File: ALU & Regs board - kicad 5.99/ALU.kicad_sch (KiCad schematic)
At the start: 50 parts, among them U1 74F381, U10 MC74ACT244DWG, U11 MC74ACT244DWG, U12 MC74ACT04DG, U13 MC74SCT00DG, U14 MC74ACT32DG, U15 MC74ACT02DG, U16 MC74ACT157DG, U17 MC74ACT153DG, U18 MC74ACT153DG, U19 MC74ACT08DG, U2 74F381, U20 MC74ACT20DG, U21 MC74ACT02DG, U22 MC74ACT02DG, U3 74F381, U4 74F382, U5 74F382, U6 74F182, U7 MC74ACT244DWG, U8 MC74ACT244DWG, U9 MC74ACT244DWG

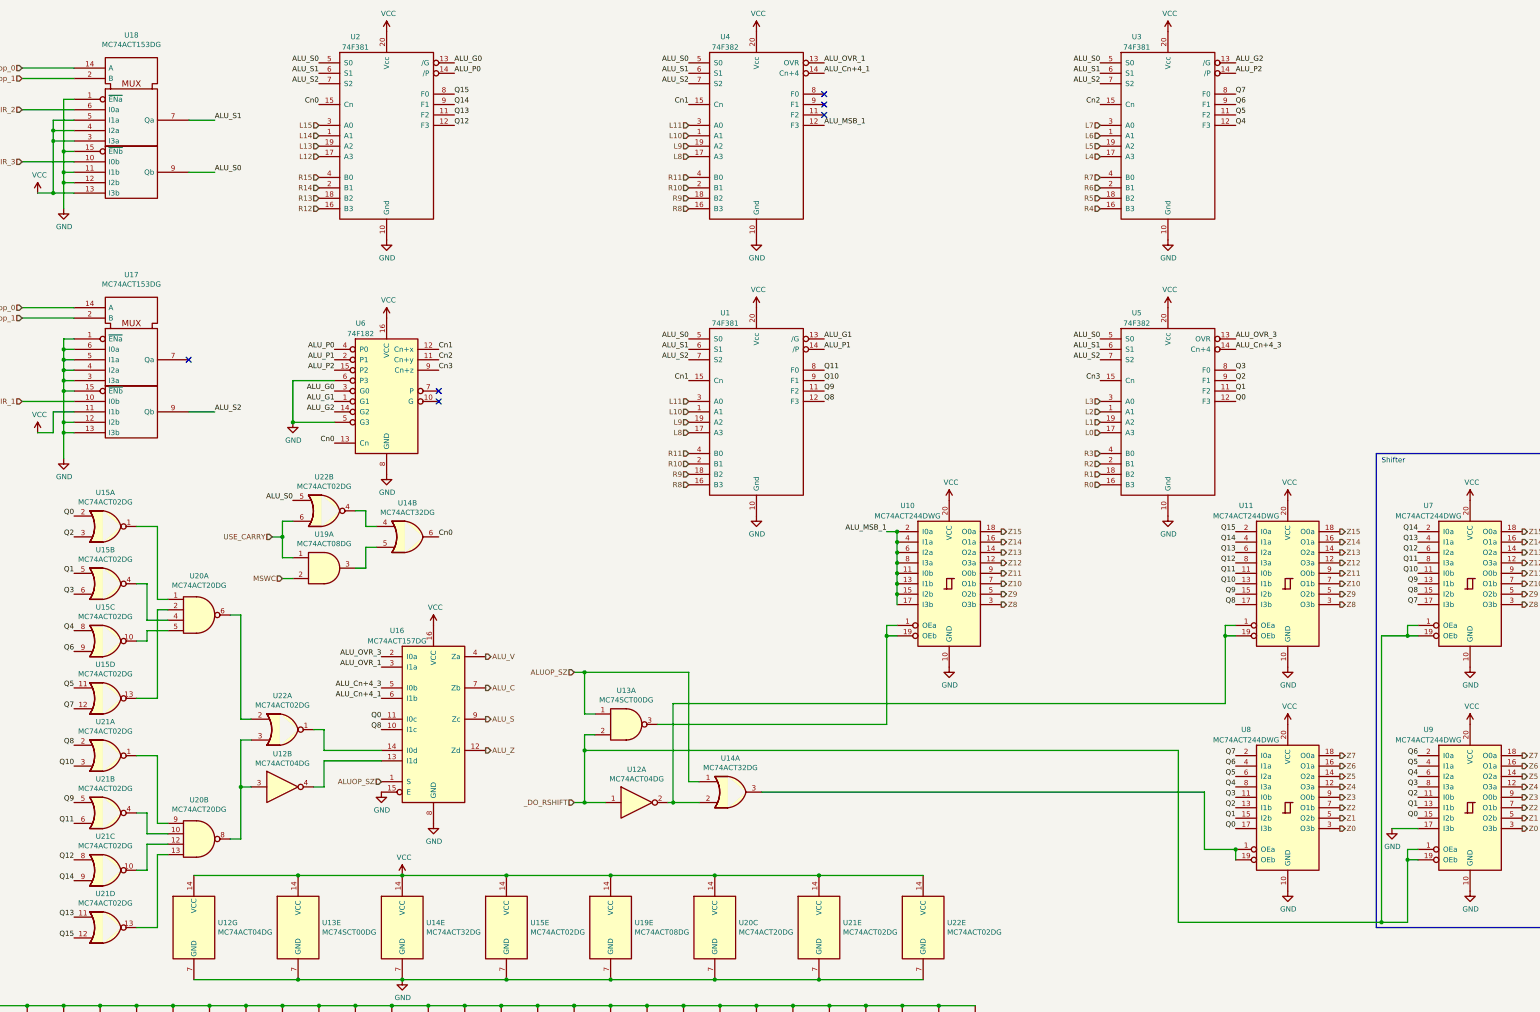
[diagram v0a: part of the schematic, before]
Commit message: added a buffer on the _RESET line, which is rather loaded
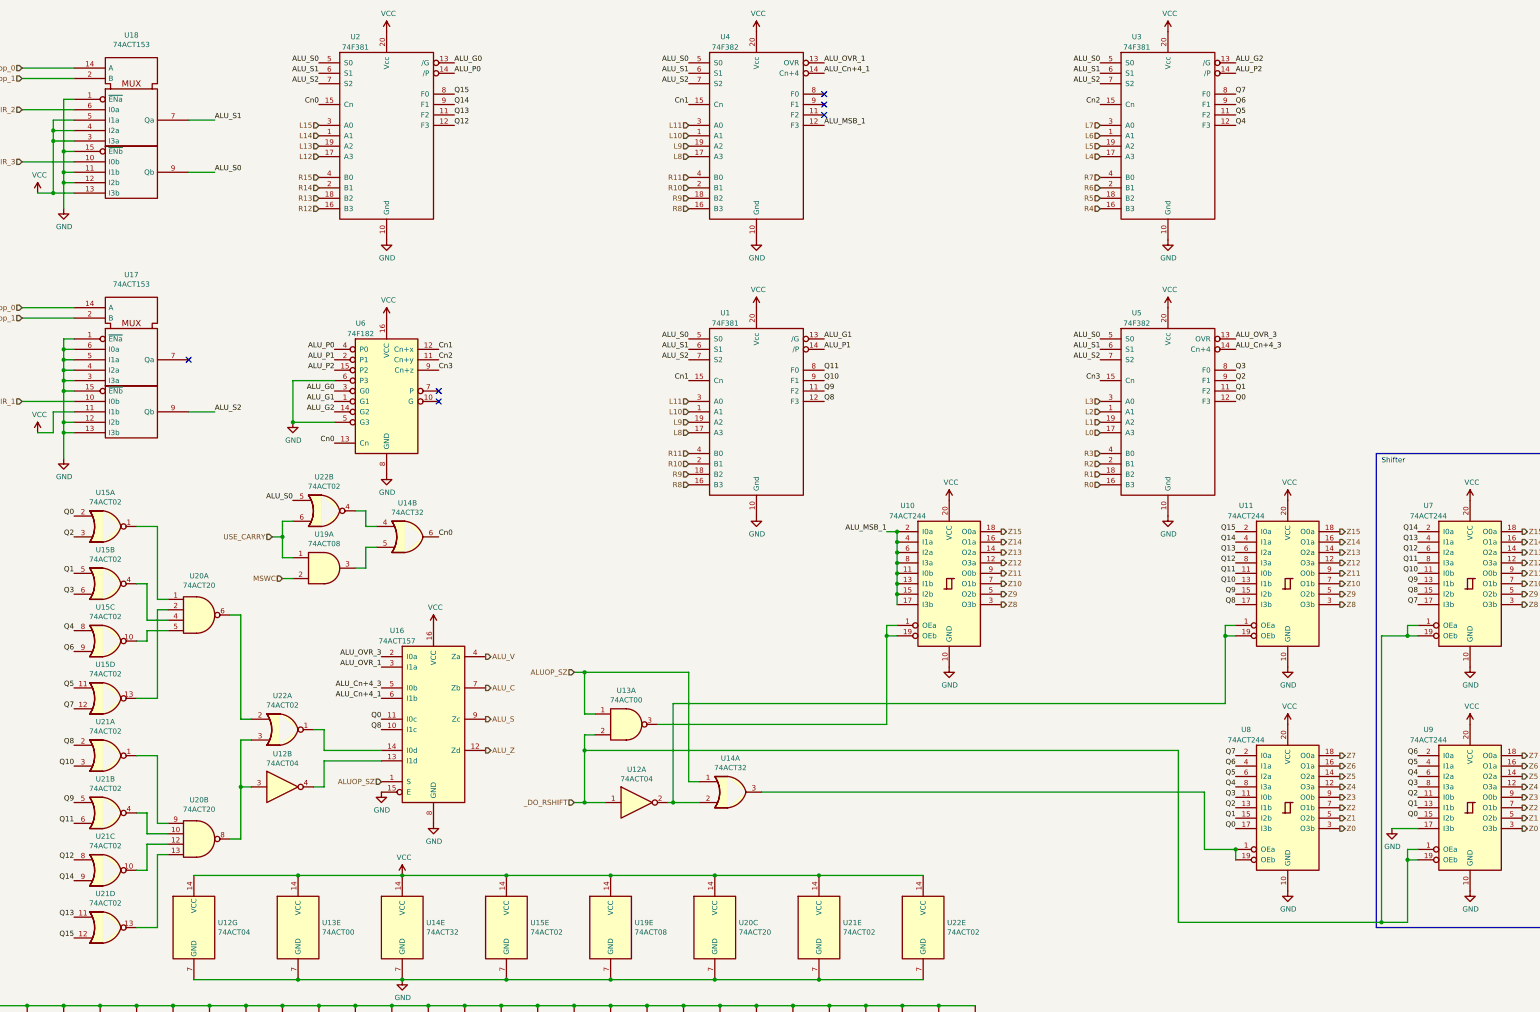
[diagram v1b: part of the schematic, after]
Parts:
- U10, U11, U7, U8, U9: value MC74ACT244DWG -> 74ACT244
- U12: value MC74ACT04DG -> 74ACT04
- U13: value MC74SCT00DG -> 74ACT00
- U14: value MC74ACT32DG -> 74ACT32
- U15, U21, U22: value MC74ACT02DG -> 74ACT02
- U16: value MC74ACT157DG -> 74ACT157
- U17, U18: value MC74ACT153DG -> 74ACT153
- U19: value MC74ACT08DG -> 74ACT08
- U20: value MC74ACT20DG -> 74ACT20
